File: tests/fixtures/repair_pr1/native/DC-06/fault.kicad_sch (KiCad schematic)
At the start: 20 parts, among them J1 TYPE-C-31-M-12, SW1 TS-1088R-02026, SW2 TS-1088R-02026, U1 ESP32-C3-WROOM-02-N4, U2 SHT30-DIS-B10KS, U3 ME6211C33R5G

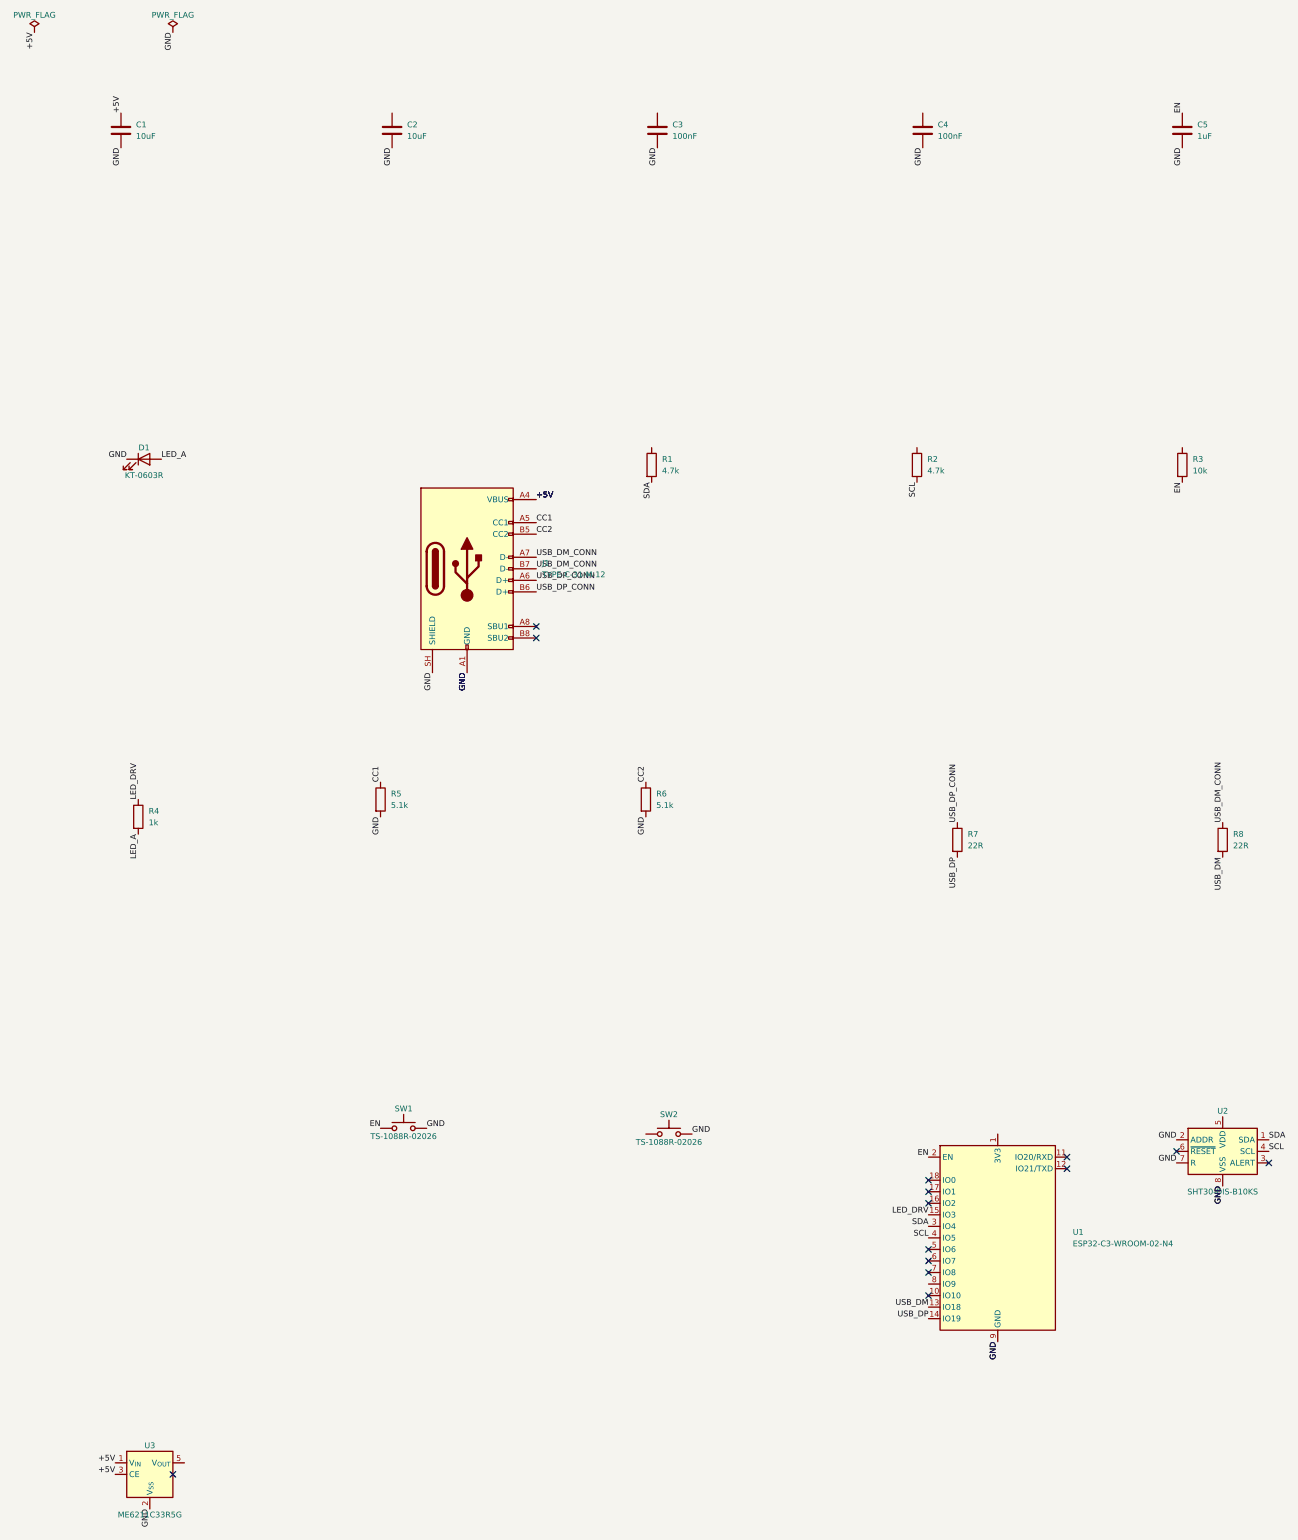
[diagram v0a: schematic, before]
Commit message: fix(benchmark): remove the DC-06/DC-04 duplicate and support multi-part synthesis
Last commit shipped a defect and it needs saying plainly. DC-06 targeted
ESP32_GPIO9_PULLUP, which is exactly DC-04's rule, on the same board, with the same
missing part. It was a near-copy: it raised the headline denominator while adding no
information, which is the worst way to grow a benchmark. DC-06 is now the R7 plus R8 USB
pair instead, so the two are distinct.

Worth being precise about what is and is not a duplicate. DC-01 and DC-03 share
USB_POLARITY_AND_SERIES and that is legitimate, because their fault families differ,
mislabelled nets versus missing components, and those are different capabilities. The
guard key includes fault_family for that reason.

Two measurements drove the redesign.

First, single-part synthesis is wrong for the USB rule. Deleting R7 breaks
USB_POLARITY_AND_SERIES, but placing R7 back does not satisfy it, because the rule
requires the R7 and R8 pair. A single-part episode is therefore wrong in both
directions. The per-part probe also shows deleting R4 breaks nothing at all, deleting C5
breaks two rules, and deleting R3 or C4 breaks several, so synthesise_fault now accepts a
list of references and repair places them all.

Second, a repair must restore every deleted label, not only the labels sitting on the
pins it restored. Deleting R7 and R8 removes the labels on all of their nets, including
the ones at the far end on U1 and J1. Restoring only the pin-sitting labels left the far
end unnamed and USB_POLARITY_AND_SERIES still failed; restoring all ten labels makes all
five rules pass. repair() now does that and the comment records the measurement.

DC-04 is now proven unrescuable rather than assumed so. Applying the frozen board's
placement record to DC-04's fixture still leaves ESP32_GPIO9_PULLUP failing, so that
fixture is not in the same coordinate frame as the frozen M2 board. Its fixture is
referenced by more than a dozen test modules, so it cannot 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
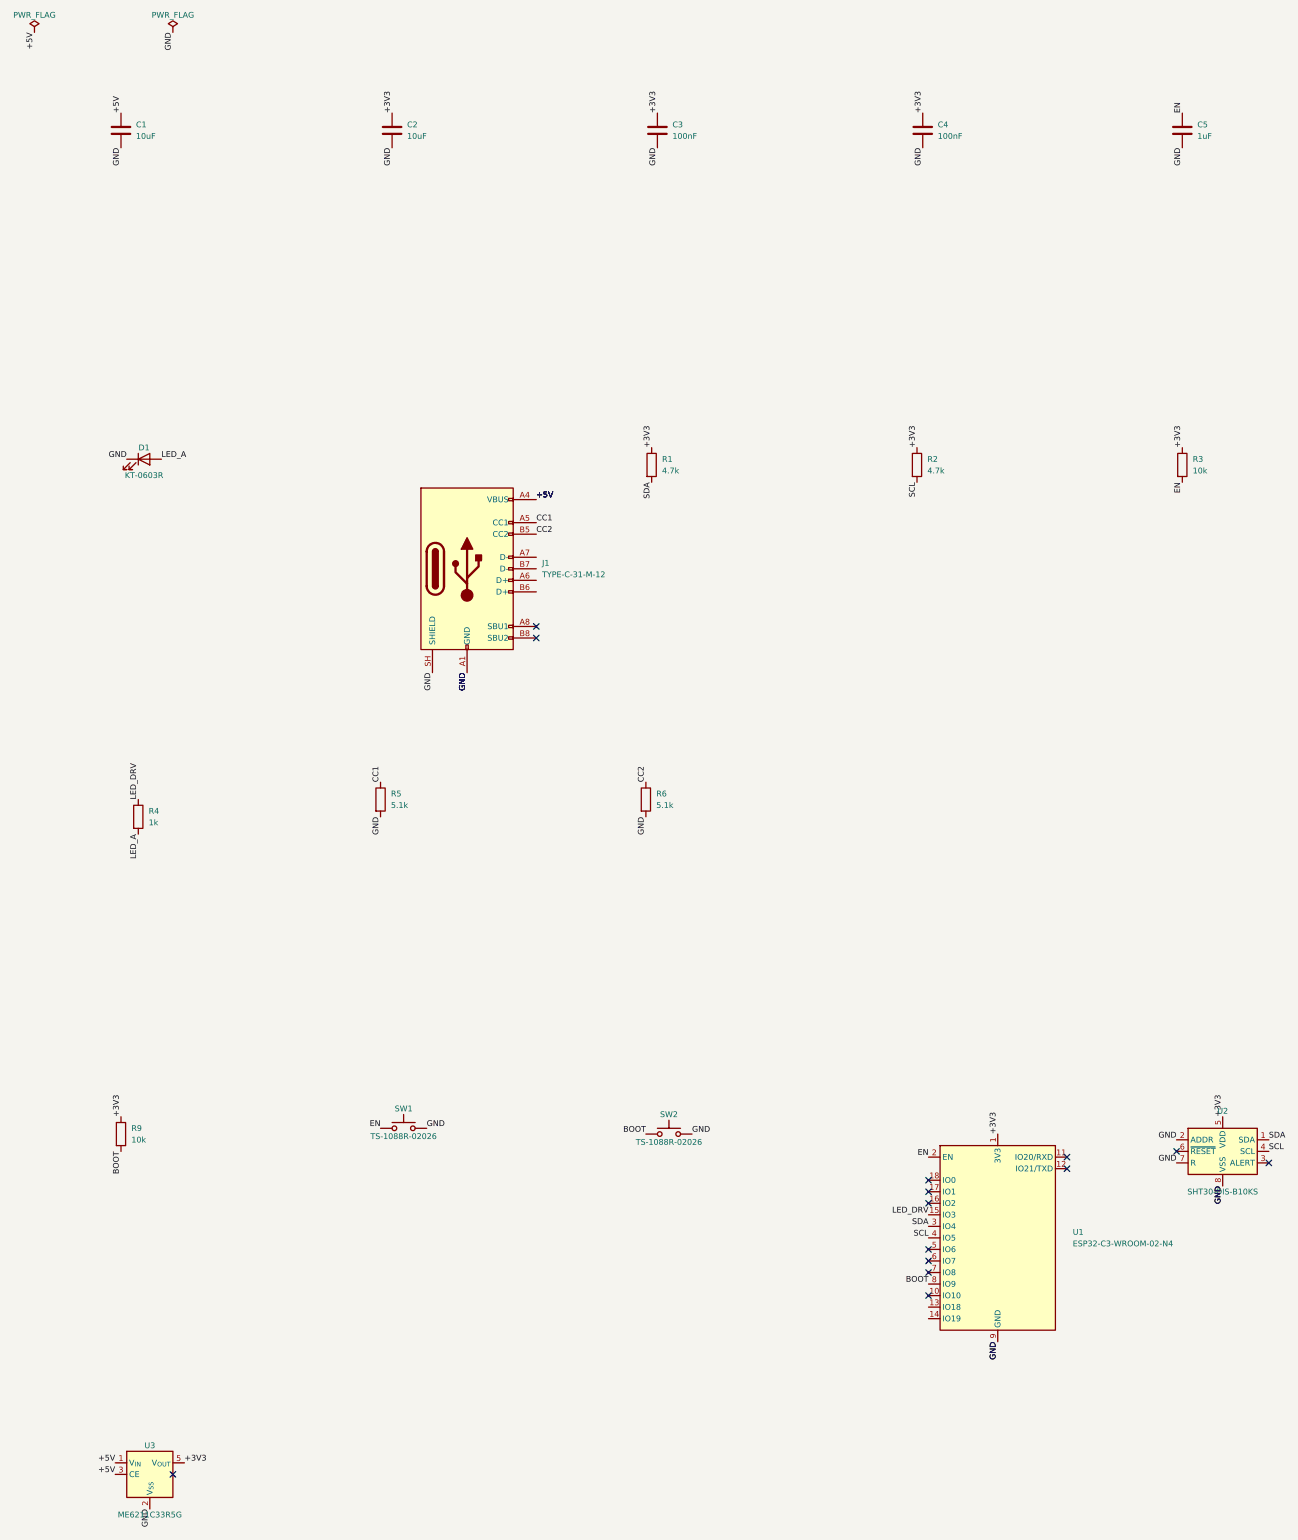
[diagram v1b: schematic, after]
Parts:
- removed R7, R8: 22R, Resistor_SMD:R_0603_1608Metric, symbol Device:R
- added R9: 10k, Resistor_SMD:R_0603_1608Metric, symbol Device:R
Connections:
- net BOOT: now reaches SW2.1
- net BOOT: now also U1.8 (IO9), R9.2
- net +3V3: now reaches U2.5 (VDD)
- net +3V3: now also C2.1, C3.1, C4.1, R1.1, R2.1, R3.1, U1.1 (3V3), U3.5 (V_{OUT}), R9.1
- net USB_DM: no longer names the net of U1.13 (IO18)
- net USB_DM_CONN: no longer names the net of J1.A7 (D-)
- net USB_DM_CONN: no longer J1.B7 (D-)
- net USB_DP: no longer names the net of U1.14 (IO19)
- net USB_DP_CONN: no longer names the net of J1.A6 (D+)
- net USB_DP_CONN: no longer J1.B6 (D+)
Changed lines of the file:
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@@
 	(property "Value" "5.1k" (at 152.146 185.42 0) (effects (font (size 1.27 1.27)) (justify left)))
 	(property "Footprint" "Resistor_SMD:R_0603_1608Metric" (at 149.86 184.15 0) (effects (font (size 1.27 1.27)) (hide yes))))
-	(symbol (lib_id "Device:R") (at 218.44 193.04 0) (unit 1) (pin "1") (pin "2") (property "Reference" "R7" (at 220.726 191.77 0) (effects (font (size 1.27 1.27)) (justify left))) (instances (project "noname" (path "/a1dbe1c3-f1f0-496b-b2c7-2a432ea67147" (reference "R7") (unit 1))))
-	(property "Value" "22R" (at 220.726 194.31 0) (effects (font (size 1.27 1.27)) (justify left)))
-	(property "Footprint" "Resistor_SMD:R_0603_1608Metric" (at 218.44 193.04 0) (effects (font (size 1.27 1.27)) (hide yes))))
-	(symbol (lib_id "Device:R") (at 276.86 193.04 0) (unit 1) (pin "1") (pin "2") (property "Reference" "R8" (at 279.146 191.77 0) (effects (font (size 1.27 1.27)) (justify left))) (instances (project "noname" (path "/a1dbe1c3-f1f0-496b-b2c7-2a432ea67147" (reference "R8") (unit 1))))
-	(property "Value" "22R" (at 279.146 194.31 0) (effects (font (size 1.27 1.27)) (justify left)))
-	(property "Footprint" "Resistor_SMD:R_0603_1608Metric" (at 276.86 193.04 0) (effects (font (size 1.27 1.27)) (hide yes))))
+	(symbol (lib_id "Device:R") (at 34.29 257.81 0) (unit 1) (pin "1") (pin "2") (property "Reference" "R9" (at 36.576 256.54 0) (effects (font (size 1.27 1.27)) (justify left))) (instances (project "noname" (path "/a1dbe1c3-f1f0-496b-b2c7-2a432ea67147" (reference "R9") (unit 1))))
+	(property "Value" "10k" (at 36.576 259.08 0) (effects (font (size 1.27 1.27)) (justify left)))
+	(property "Footprint" "Resistor_SMD:R_0603_1608Metric" (at 34.29 257.81 0) (effects (font (size 1.27 1.27)) (hide yes))))
 	(symbol (lib_id "Switch:SW_Push") (at 96.52 256.54 0) (unit 1) (pin "1") (pin "2") (property "Reference" "SW1" (at 96.52 252.222 0) (effects (font (size 1.27 1.27)))) (instances (project "noname" (path "/a1dbe1c3-f1f0-496b-b2c7-2a432ea67147" (reference "SW1") (unit 1))))
 	(property "Value" "TS-1088R-02026" (at 96.52 258.318 0) (effects (font (size 1.27 1.27)))))
@@
 	(symbol (lib_id "power:PWR_FLAG") (at 45.72 15.24 0) (unit 1) (pin "1") (property "Reference" "#FLG02" (at 45.72 16.51 0) (effects (font (size 1.27 1.27)) (hide yes))) (instances (project "noname" (path "/a1dbe1c3-f1f0-496b-b2c7-2a432ea67147" (reference "#FLG02") (unit 1))))
 	(property "Value" "PWR_FLAG" (at 45.72 11.43 0) (effects (font (size 1.27 1.27)))))
+	(label "+3V3" (at 93.98 33.02 90) (effects (font (size 1.27 1.27)) (justify left bottom)))
+	(label "+3V3" (at 152.4 33.02 90) (effects (font (size 1.27 1.27)) (justify left bottom)))
+	(label "+3V3" (at 210.82 33.02 90) (effects (font (size 1.27 1.27)) (justify left bottom)))
+	(label "+3V3" (at 151.13 106.68 90) (effects (font (size 1.27 1.27)) (justify left bottom)))
+	(label "+3V3" (at 209.55 106.68 90) (effects (font (size 1.27 1.27)) (justify left bottom)))
+	(label "+3V3" (at 267.97 106.68 90) (effects (font (size 1.27 1.27)) (justify left bottom)))
+	(label "+3V3" (at 34.29 254 90) (effects (font (size 1.27 1.27)) (justify left bottom)))
+	(label "+3V3" (at 227.33 257.81 90) (effects (font (size 1.27 1.27)) (justify left bottom)))
+	(label "+3V3" (at 276.86 254 90) (effects (font (size 1.27 1.27)) (justify left bottom)))
+	(label "+3V3" (at 48.26 330.2 0) (effects (font (size 1.27 1.27)) (justify left bottom)))
 	(label "+5V" (at 34.29 33.02 90) (effects (font (size 1.27 1.27)) (justify left bottom)))
 	(label "+5V" (at 125.73 118.11 0) (effects (font (size 1.27 1.27)) (justify left bottom)))
@@
 	(label "+5V" (at 33.02 330.2 180) (effects (font (size 1.27 1.27)) (justify right bottom)))
 	(label "+5V" (at 33.02 332.74 180) (effects (font (size 1.27 1.27)) (justify right bottom)))
+	(label "BOOT" (at 34.29 261.62 270) (effects (font (size 1.27 1.27)) (justify right bottom)))
+	(label "BOOT" (at 149.86 257.81 180) (effects (font (size 1.27 1.27)) (justify right bottom)))
+	(label "BOOT" (at 212.09 290.83 180) (effects (font (size 1.27 1.27)) (justify right bottom)))
 	(label "CC1" (at 125.73 123.19 0) (effects (font (size 1.27 1.27)) (justify left bottom)))
 	(label "CC1" (at 91.44 180.34 90) (effects (font (size 1.27 1.27)) (justify left bottom)))
@@
 	(label "SDA" (at 212.09 278.13 180) (effects (font (size 1.27 1.27)) (justify right bottom)))
 	(label "SDA" (at 287.02 259.08 0) (effects (font (size 1.27 1.27)) (justify left bottom)))
-	(label "USB_DM" (at 276.86 196.85 270) (effects (font (size 1.27 1.27)) (justify right bottom)))
-	(label "USB_DM" (at 212.09 295.91 180) (effects (font (size 1.27 1.27)) (justify right bottom)))
-	(label "USB_DM_CONN" (at 125.73 130.81 0) (effects (font (size 1.27 1.27)) (justify left bottom)))
-	(label "USB_DM_CONN" (at 125.73 133.35 0) (effects (font (size 1.27 1.27)) (justify left bottom)))
-	(label "USB_DM_CONN" (at 276.86 189.23 90) (effects (font (size 1.27 1.27)) (justify left bottom)))
-	(label "USB_DP" (at 218.44 196.85 270) (effects (font (size 1.27 1.27)) (justify right bottom)))
-	(label "USB_DP" (at 212.09 298.45 180) (effects (font (size 1.27 1.27)) (justify right bottom)))
-	(label "USB_DP_CONN" (at 125.73 135.89 0) (effects (font (size 1.27 1.27)) (justify left bottom)))
-	(label "USB_DP_CONN" (at 125.73 138.43 0) (effects (font (size 1.27 1.27)) (justify left bottom)))
-	(label "USB_DP_CONN" (at 218.44 189.23 90) (effects (font (size 1.27 1.27)) (justify left bottom)))
 	(label "+5V" (at 15.24 15.24 270) (effects (font (size 1.27 1.27)) (justify right bottom)))
 	(label "GND" (at 45.72 15.24 270) (effects (font (size 1.27 1.27)) (justify right bottom)))
